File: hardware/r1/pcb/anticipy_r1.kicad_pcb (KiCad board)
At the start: 4 copper layers, 47 x 18 mm, 45 parts, among them J1 USB4105-GF-A, J2 BATT, J3 MOTOR, J4 TC2030-IDC-NL, Q1 2N7002, SW1 EVQ-P7C01P, U1 MDBT50Q-1MV2, U2 BQ24075RGT, U3 AP2112K-3.3, U4 USBLC6-2SC6, U5 W25Q128JVSIQ, U6 LIS2DH12TR

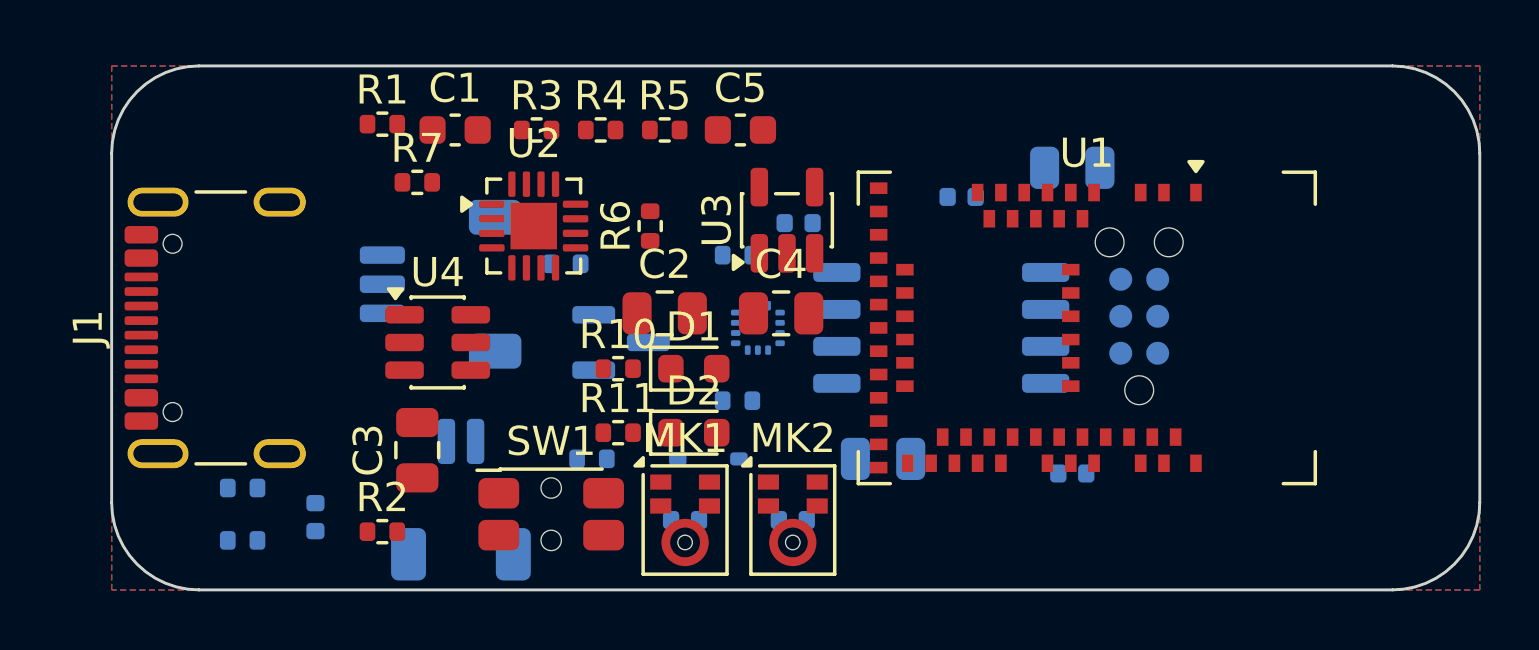
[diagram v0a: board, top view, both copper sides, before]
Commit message: hardware/r1: fully routed 4-layer PCB, DRC clean (0 violations, 0 unconnected)
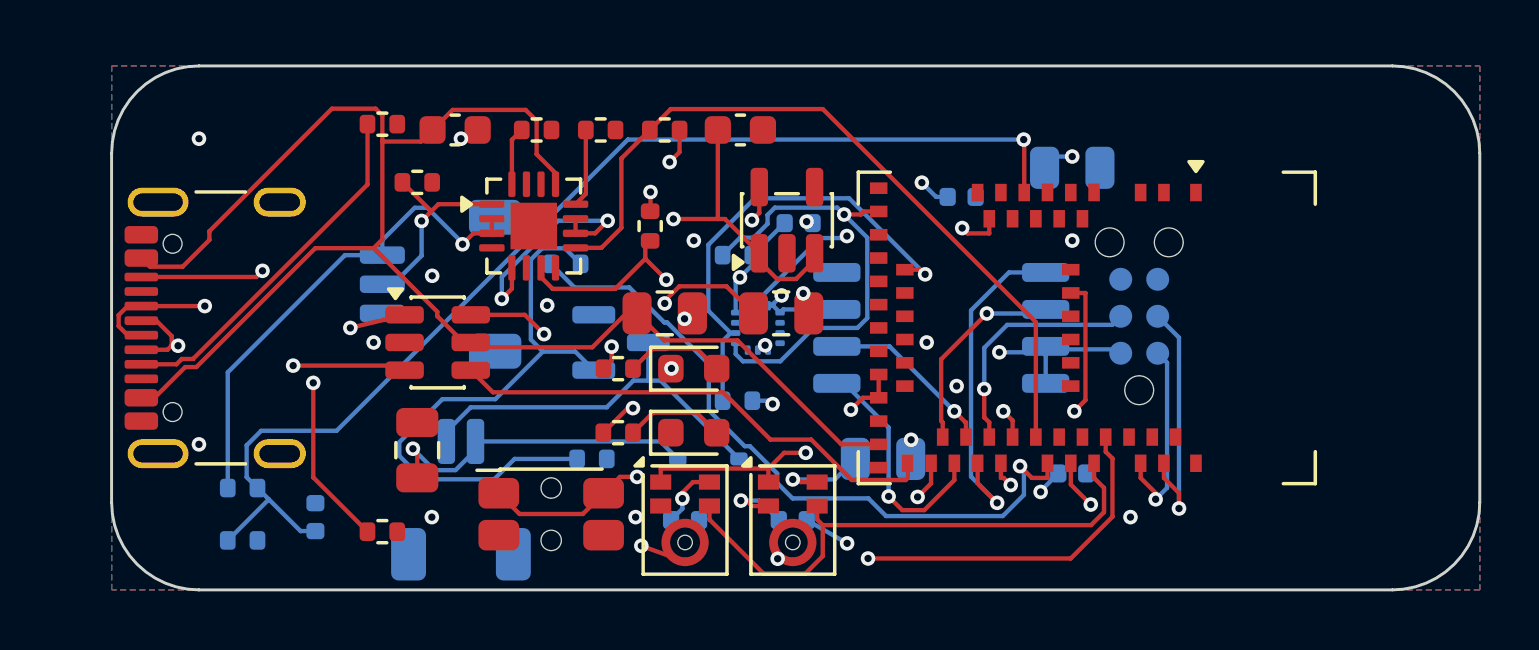
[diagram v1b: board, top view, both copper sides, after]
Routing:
- net VBUS_5V: track 0.00 -> 55.3 mm
- net VBAT_SENSE: track 0.00 -> 39.1 mm, vias 0 -> 1
- net VSYS: track 0.00 -> 37.6 mm, vias 0 -> 4
- net BTN: track 0.00 -> 30.9 mm, vias 0 -> 2
- net +3V3: track 0.00 -> 29.2 mm, vias 0 -> 14
- net VBAT: track 0.00 -> 28.4 mm, vias 0 -> 2
- net nPGOOD: track 0.00 -> 26.2 mm, vias 0 -> 2
- net nCHG_STAT: track 0.00 -> 26.2 mm
- net HAPTIC_EN: track 0.00 -> 23.9 mm, vias 0 -> 1
- net PDM_DATA: track 0.00 -> 22.5 mm, vias 0 -> 2
- net HAPTIC_G: track 0.00 -> 20.9 mm
- net USB_DP: track 0.00 -> 19.4 mm, vias 0 -> 2
- net PDM_CLK: track 0.00 -> 18.8 mm
- net LED_RED: track 0.00 -> 18.4 mm, vias 0 -> 3
- net USB_DN: track 0.00 -> 17.1 mm
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
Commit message: hardware/r1: fit 32 MB Macronix NOR (U5) on the verified layout
U5 W25Q128JVSIQ (16 MB) -> MX25L25645GMI-08G (256 Mbit / 32 MB) in the same
SOP-8 208-mil pattern, so placement and routing are untouched: 0 DRC
violations, 0 unconnected, 0 parity issues, ERC clean (4 intentional
warnings: PDM mics sharing DATA, /WP + /HOLD tied high).

Winbond has no >16 MB part in this footprint (WSON-8 8x6 or SOIC-16 300-mil
only); the WSON attempt collided with C4/J4 and shorted copper under the old
body to the thermal pad. docs/STORAGE.md records that and the runtime math:
32 MB is 4.3 h at 16 kbps, not 16 h, so the flash stays a BLE-offload buffer
and standalone 16 h needs the r1b SPI NAND.

Firmware: 4-byte addressing above 128 Mbit (EN4B 0xB7 or 0x13/0x12/0xDC),
JEDEC ID C2 20 19.
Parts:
- U5: value W25Q128JVSIQ -> MX25L25645GMI-08G
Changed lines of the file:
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@@
 			)
 		)
-		(property "Value" "W25Q128JVSIQ"
+		(property "Value" "MX25L25645GMI-08G"
 			(at 0 -3.6 180)
 			(layer "B.Fab")

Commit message: hardware/r1: fix U6 part number to LIS2DHTR, add JLCPCB BOM with LCSC codes
U6 used the LGA-14 2x2 footprint and LIS2DH symbol pinout while the BOM called out LIS2DH12TR, an LGA-12 part with a different pin order (pin 2 is CS, not SDA). Placed part is now LIS2DHTR (LCSC C155670, in stock); no footprint, placement or routing change.

anticipy_r1_bom_jlcpcb.csv maps every line to an LCSC code for PCBA. U1 (Raytac MDBT50Q-1MV2) has zero JLC stock so it must be consigned or hand soldered; J4 is Tag-Connect pads with no part to place.
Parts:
- U6: value LIS2DH12TR -> LIS2DHTR
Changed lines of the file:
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@@
 			)
 		)
-		(property "Value" "LIS2DH12TR"
+		(property "Value" "LIS2DHTR"
 			(at 0 -1.8 180)
 			(layer "B.Fab")
